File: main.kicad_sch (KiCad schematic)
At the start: 30 parts, among them J1 USB_C_Receptacle_USB2.0_16P, J2 Conn_ARM_JTAG_SWD_10, U1 XC6206PxxxMR, U2 USBLC6-2SC6, U3 CH340N, U4 E73-2G4M04S1B

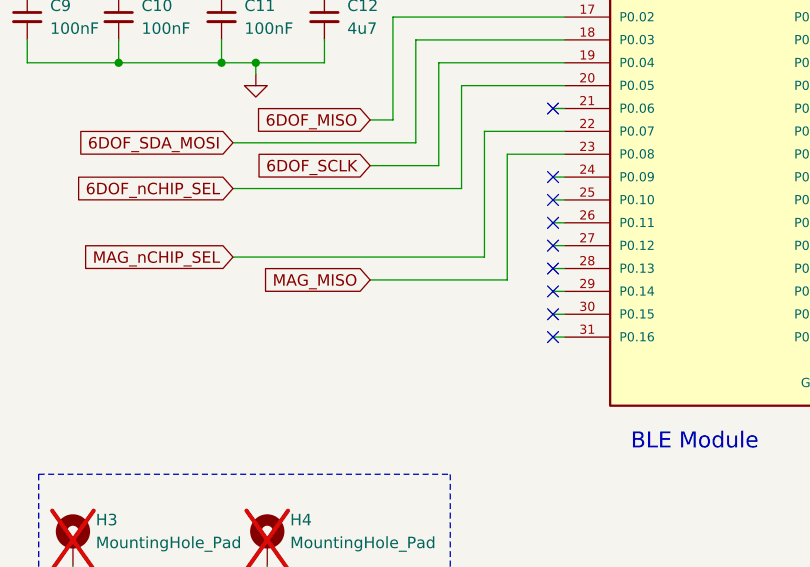
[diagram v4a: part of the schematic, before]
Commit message: Brought out INT pin from magnetometer to MCU, in case of need.  Updated layout accordingly
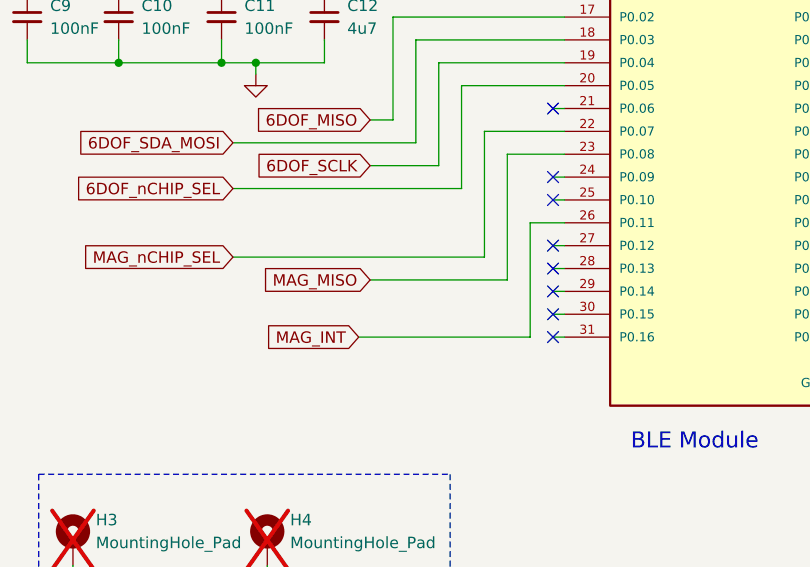
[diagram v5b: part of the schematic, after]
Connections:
- net MAG_INT: now reaches U4.26 (P0.11)
- no-connect marks 21 -> 20
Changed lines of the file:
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@@
-	)
-	(no_connect
-		(at 184.15 128.27)
 	)
 	(no_connect
@@
 	(wire
 		(pts
+			(xy 181.61 140.97) (xy 162.56 140.97)
+		)
+		(stroke
+			(width 0)
+			(type default)
+		)
+	)
+	(wire
+		(pts
 			(xy 96.52 67.31) (xy 96.52 68.58)
 		)
@@
 	(wire
 		(pts
+			(xy 181.61 128.27) (xy 181.61 140.97)
+		)
+		(stroke
+			(width 0)
+			(type default)
+		)
+	)
+	(wire
+		(pts
 			(xy 184.15 123.19) (xy 185.42 123.19)
 		)
@@
 	(wire
 		(pts
-			(xy 184.15 128.27) (xy 185.42 128.27)
+			(xy 181.61 128.27) (xy 185.42 128.27)
 		)
 		(stroke
@@
 				(hide yes)
 			)
+		)
+	)
+	(global_label "MAG_INT"
+		(shape input)
+		(at 162.56 140.97 180)
+		(fields_autoplaced yes)
+		(effects
+			(font
+				(size 1.27 1.27)
+			)
+			(justify right)
+		)
+		(property "Intersheetrefs" "${INTERSHEET_REFS}"
+			(at 151.8943 140.97 0)
+			(effects
+				(font
+					(size 1.27 1.27)
+				)
+				(justify right)
+				(hide yes)
+			)

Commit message: Exported BOM, pick-and-place files.  Finalized schematic and exported PDF.  Files used to place JLCPCB order
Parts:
- C1, C12, C2, C3, C4, C8: Manufacturer Samsung Electro-Mechanics -> Samsung Electro-Mechanics
- U4: LCSC Part # (none) -> C411306; LSCS Part # C411306 -> (none)
